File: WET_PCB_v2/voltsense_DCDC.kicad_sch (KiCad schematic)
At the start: 9 parts, among them J18 Capacitor connector, J20 Capacitor connector, U3 Opamp_Quad

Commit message: notees
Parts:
- removed D23, D24: 1N4004, Diode_THT:D_DO-15_P2.54mm_Vertical_CathodeUp, symbol Diode:1N4004
- added D29, D30: D_Zener, Diode_THT:D_DO-15_P2.54mm_Vertical_CathodeUp, symbol Device:D_Zener
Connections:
- net GND: now also D29.2 (A)
- net VDD_OPAMP: now also D30.1 (K)
- net Vsense_ADC: now also D29.1 (K), D30.2 (A)
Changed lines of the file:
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@@
+	)
+	(symbol
+		(lib_id "Device:D_Zener")
+		(at 121.92 58.42 270)
+		(unit 1)
+		(body_style 1)
+		(exclude_from_sim no)
+		(in_bom yes)
+		(on_board yes)
+		(in_pos_files yes)
+		(dnp no)
+		(fields_autoplaced yes)
+		(property "Reference" "D30"
+			(at 124.46 57.1499 90)
+			(show_name no)
+			(do_not_autoplace no)
+			(effects
+				(font
+					(size 1.27 1.27)
+				)
+				(justify left)
+			)
+		)
+		(property "Value" "D_Zener"
+			(at 124.46 59.6899 90)
+			(show_name no)
+			(do_not_autoplace no)
+			(effects
+				(font
+					(size 1.27 1.27)
+				)
+				(justify left)
+			)
+		)
+		(property "Footprint" "Diode_THT:D_DO-15_P2.54mm_Vertical_CathodeUp"
+			(at 121.92 58.42 0)
+			(hide yes)
+			(show_name no)
+			(do_not_autoplace no)
+			(effects
+				(font
+					(size 1.27 1.27)
+				)
+			)
+		)
+		(property "Datasheet" ""
+			(at 121.92 58.42 0)
+			(hide yes)
+			(show_name no)
+			(do_not_autoplace no)
+			(effects
+				(font
+					(size 1.27 1.27)
+				)
+			)
+		)
+		(property "Description" "Zener diode"
+			(at 121.92 58.42 0)
+			(hide yes)
+			(show_name no)
+			(do_not_autoplace no)
+			(effects
+				(font
+					(size 1.27 1.27)
+				)
+			)
+		)
+		(pin "2"
+		)
+		(pin "1"
+		)
+		(instances
+			(project "WET_PCB_v2"
+				(path "/13451c35-1666-47d9-9525-8d8125ba1cf3/a17383a4-d27f-4c25-9e0c-b0df1856b8d8"
+					(reference "D30")
+					(unit 1)
+				)
+			)
+		)
 	)
 	(symbol
@@
 				(path "/13451c35-1666-47d9-9525-8d8125ba1cf3/a17383a4-d27f-4c25-9e0c-b0df1856b8d8"
 					(reference "#PWR056")
-					(unit 1)
-				)
-			)
-		)
-	)
-	(symbol
-		(lib_id "Diode:1N4004")
-		(at 121.92 68.58 90)
-		(mirror x)
-		(unit 1)
-		(body_style 1)
-		(exclude_from_sim no)
-		(in_bom yes)
-		(on_board yes)
-		(in_pos_files yes)
-		(dnp no)
-		(fields_autoplaced yes)
-		(property "Reference" "D24"
-			(at 124.46 67.3099 90)
-			(show_name no)
-			(do_not_autoplace no)
-			(effects
-				(font
-					(size 1.27 1.27)
-				)
-				(justify right)
-			)
-		)
-		(property "Value" "1N4004"
-			(at 124.46 69.8499 90)
-			(show_name no)
-			(do_not_autoplace no)
-			(effects
-				(font
-					(size 1.27 1.27)
-				)
-				(justify right)
-			)
-		)
-		(property "Footprint" "Diode_THT:D_DO-15_P2.54mm_Vertical_CathodeUp"
-			(at 126.365 68.58 0)
-			(hide yes)
-			(show_name no)
-			(do_not_autoplace no)
-			(effects
-				(font
-					(size 1.27 1.27)
-				)
-			)
-		)
-		(property "Datasheet" "http://www.vishay.com/docs/88503/1n4001.pdf"
-			(at 121.92 68.58 0)
-			(hide yes)
-			(show_name no)
-			(do_not_autoplace no)
-			(effects
-				(font
-					(size 1.27 1.27)
-				)
-			)
-		)
-		(property "Description" "400V 1A General Purpose Rectifier Diode, DO-41"
-			(at 121.92 68.58 0)
-			(hide yes)
-			(show_name no)
-			(do_not_autoplace no)
-			(effects
-				(font
-					(size 1.27 1.27)
-				)
-			)
-		)
-		(property "Sim.Device" "D"
-			(at 121.92 68.58 0)
-			(hide yes)
-			(show_name no)
-			(do_not_autoplace no)
-			(effects
-				(font
-					(size 1.27 1.27)
-				)
-			)
-		)
-		(property "Sim.Pins" "1=K 2=A"
-			(at 121.92 68.58 0)
-			(hide yes)
-			(show_name no)
-			(do_not_autoplace no)
-			(effects
-				(font
-					(size 1.27 1.27)
-				)
-			)
-		)
-		(pin "1"
-		)
-		(pin "2"
-		)
-		(instances
-			(project "WET_PCB_v2"
-				(path "/13451c35-1666-47d9-9525-8d8125ba1cf3/a17383a4-d27f-4c25-9e0c-b0df1856b8d8"
-					(reference "D24")
 					(unit 1)
 				)
@@
 	)
 	(symbol
+		(lib_id "Device:D_Zener")
+		(at 121.92 68.58 270)
+		(unit 1)
+		(body_style 1)
+		(exclude_from_sim no)
+		(in_bom yes)
+		(on_board yes)
+		(in_pos_files yes)
+		(dnp no)
+		(fields_autoplaced yes)
+		(property "Reference" "D29"
+			(at 124.46 67.3099 90)
+			(show_name no)
+			(do_not_autoplace no)
+			(effects
+				(font
+					(size 1.27 1.27)
+				)
+				(justify left)
+			)
+		)
+		(property "Value" "D_Zener"
+			(at 124.46 69.8499 90)
+			(show_name no)
+			(do_not_autoplace no)
+			(effects
+				(font
+					(size 1.27 1.27)
+				)
+				(justify left)
+			)
+		)
+		(property "Footprint" "Diode_THT:D_DO-15_P2.54mm_Vertical_CathodeUp"
+			(at 121.92 68.58 0)
+			(hide yes)
+			(show_name no)
+			(do_not_autoplace no)
+			(effects
+				(font
+					(size 1.27 1.27)
+				)
+			)
+		)
+		(property "Datasheet" ""
+			(at 121.92 68.58 0)
+			(hide yes)
+			(show_name no)
+			(do_not_autoplace no)
+			(effects
+				(font
+					(size 1.27 1.27)
+				)
+			)
+		)
+		(property "Description" "Zener diode"
+			(at 121.92 68.58 0)
+			(hide yes)
+			(show_name no)
+			(do_not_autoplace no)
+			(effects
+				(font
+					(size 1.27 1.27)
+				)
+			)
+		)
+		(pin "2"
+		)
+		(pin "1"
+		)
+		(instances
+			(project "WET_PCB_v2"
+				(path "/13451c35-1666-47d9-9525-8d8125ba1cf3/a17383a4-d27f-4c25-9e0c-b0df1856b8d8"
+					(reference "D29")
+					(unit 1)
+				)
+			)
+		)
+	)
+	(symbol
 		(lib_id "power:GND")
 		(at 55.88 77.47 0)
@@
 					(unit 1)
 				)
-			)
-		)
-	)
-	(symbol
-		(lib_id "Diode:1N4004")
-		(at 121.92 58.42 90)
-		(mirror x)
-		(unit 1)
-		(body_style 1)
-		(exclude_from_sim no)
-		(in_bom yes)
-		(on_board yes)
-		(in_pos_files yes)
-		(dnp no)
-		(fields_autoplaced yes)
-		(property "Reference" "D23"
-			(at 124.46 57.1499 90)
-			(show_name no)
-			(do_not_autoplace no)
-			(effects
-				(font
-					(size 1.27 1.27)
-				)
-				(justify right)
-			)
-		)
-		(property "Value" "1N4004"
-			(at 124.46 59.6899 90)
-			(show_name no)
-			(do_not_autoplace no)
-			(effects
-				(font
-					(size 1.27 1.27)
-				)
-				(justify right)
-			)
-		)
-		(property "Footprint" "Diode_THT:D_DO-15_P2.54mm_Vertical_CathodeUp"
-			(at 126.365 58.42 0)
-			(hide yes)
-			(show_name no)
-			(do_not_autoplace no)
-			(effects
-				(font
-					(size 1.27 1.27)
-				)
-			)
-		)
-		(property "Datasheet" "http://www.vishay.com/docs/88503/1n4001.pdf"
-			(at 121.92 58.42 0)
-			(hide yes)
-			(show_name no)
-			(do_not_autoplace no)
-			(effects
-				(font
-					(size 1.27 1.27)
-				)
-			)
-		)
-		(property "Description" "400V 1A General Purpose Rectifier Diode, DO-41"
-			(at 121.92 58.42 0)
-			(hide yes)
-			(show_name no)
-			(do_not_autoplace no)
-			(effects
-				(font
-					(size 1.27 1.27)
-				)
-			)
-		)
-		(property "Sim.Device" "D"
-			(at 121.92 58.42 0)
-			(hide yes)
-			(show_name no)
-			(do_not_autoplace no)
-			(effects
-				(font
-					(size 1.27 1.27)
-				)
-			)
-		)
-		(property "Sim.Pins" "1=K 2=A"
-			(at 121.92 58.42 0)
-			(hide yes)
-			(show_name no)
-			(do_not_autoplace no)
-			(effects
-				(font
-					(size 1.27 1.27)
-				)
-			)
-		)
-		(pin "1"
-		)
-		(pin "2"
-		)
-		(instances
-			(project "WET_PCB_v2"
-				(path "/13451c35-1666-47d9-9525-8d8125ba1cf3/a17383a4-d27f-4c25-9e0c-b0df1856b8d8"
-					(reference "D23")
-					(unit 1)
-				)

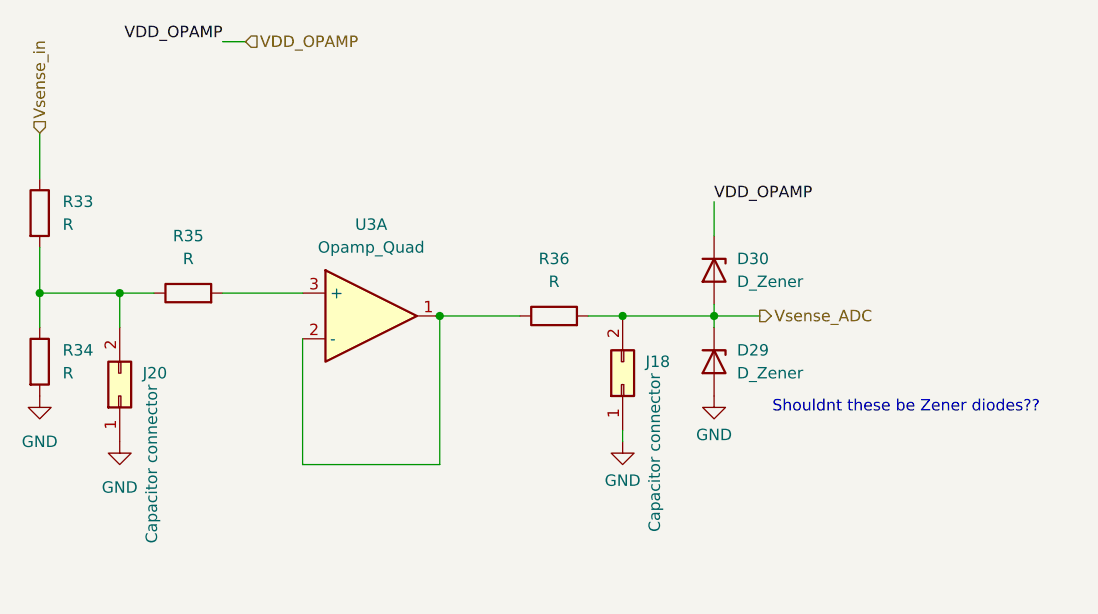
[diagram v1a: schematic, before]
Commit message: redid part of layout inverter
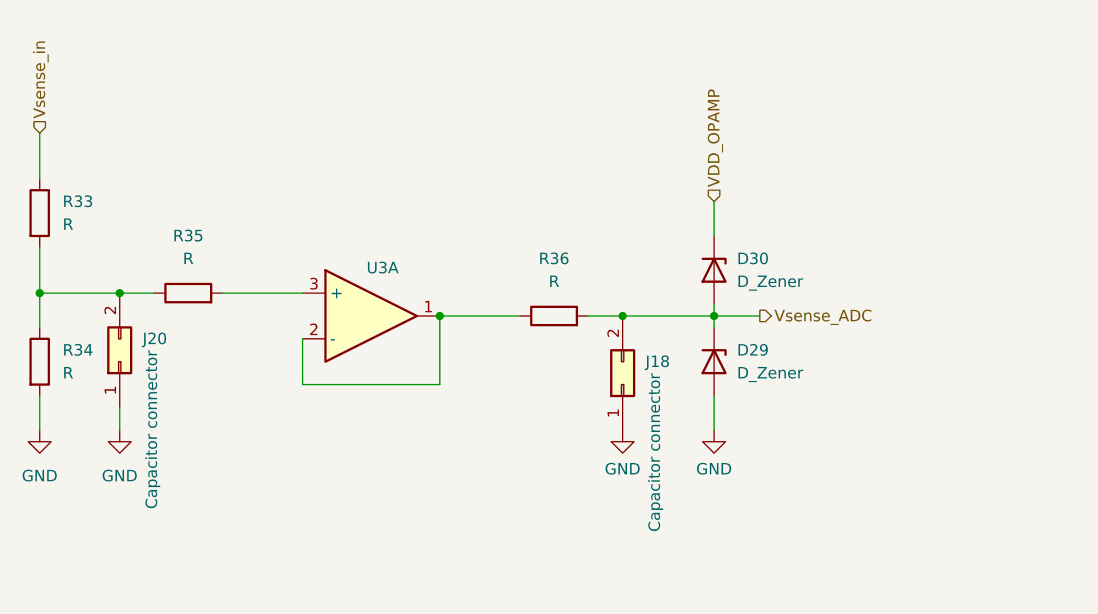
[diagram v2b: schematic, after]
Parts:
- R33, R34, R35, R36: footprint Resistor_THT:R_Axial_DIN0207_L6.3mm_D2.5mm_P7.62mm_Horizontal -> Resistor_SMD:R_0805_2012Metric_Pad1.20x1.40mm_HandSolder
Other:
- note removed: "Shouldnt these be Zener diodes??"
- moved on the sheet: J20
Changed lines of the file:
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@@
 	(generator_version "10.0")
 	(paper "A4")
-	(text "Shouldnt these be Zener diodes??\n"
-		(exclude_from_sim no)
-		(at 143.256 73.66 0)
-		(effects
-			(font
-				(size 1.27 1.27)
-			)
-		)
+	(junction
+		(at 121.92 63.5)
+		(diameter 0)
+		(color 0 0 0 0)
+	)
+	(junction
+		(at 91.44 63.5)
+		(diameter 0)
+		(color 0 0 0 0)
+	)
+	(junction
+		(at 111.76 63.5)
+		(diameter 0)
+		(color 0 0 0 0)
+	)
+	(junction
+		(at 46.99 60.96)
+		(diameter 0)
+		(color 0 0 0 0)
 	)
 	(junction
@@
 		(color 0 0 0 0)
 	)
-	(junction
-		(at 121.92 63.5)
-		(diameter 0)
-		(color 0 0 0 0)
-	)
-	(junction
-		(at 91.44 63.5)
-		(diameter 0)
-		(color 0 0 0 0)
-	)
-	(junction
-		(at 111.76 63.5)
-		(diameter 0)
-		(color 0 0 0 0)
-	)
-	(junction
-		(at 46.99 60.96)
-		(diameter 0)
-		(color 0 0 0 0)
-	)
-	(wire
-		(pts
-			(xy 91.44 63.5) (xy 91.44 80.01)
-		)
-		(stroke
-			(width 0)
-			(type default)
-		)
-	)
-	(wire
-		(pts
-			(xy 69.85 33.02) (xy 67.31 33.02)
+	(wire
+		(pts
+			(xy 46.99 72.39) (xy 46.99 76.2)
+		)
+		(stroke
+			(width 0)
+			(type default)
+		)
+	)
+	(wire
+		(pts
+			(xy 91.44 63.5) (xy 91.44 71.12)
 		)
 		(stroke
@@
 	(wire
 		(pts
+			(xy 55.88 73.66) (xy 55.88 76.2)
+		)
+		(stroke
+			(width 0)
+			(type default)
+		)
+	)
+	(wire
+		(pts
 			(xy 121.92 50.8) (xy 121.92 54.61)
 		)
@@
 	(wire
 		(pts
-			(xy 55.88 60.96) (xy 55.88 64.77)
-		)
-		(stroke
-			(width 0)
-			(type default)
-		)
-	)
-	(wire
-		(pts
 			(xy 121.92 63.5) (xy 121.92 64.77)
 		)
@@
 	(wire
 		(pts
-			(xy 111.76 76.2) (xy 111.76 77.47)
-		)
-		(stroke
-			(width 0)
-			(type default)
-		)
-	)
-	(wire
-		(pts
 			(xy 55.88 60.96) (xy 59.69 60.96)
 		)
@@
 	(wire
 		(pts
+			(xy 121.92 76.2) (xy 121.92 72.39)
+		)
+		(stroke
+			(width 0)
+			(type default)
+		)
+	)
+	(wire
+		(pts
 			(xy 111.76 63.5) (xy 121.92 63.5)
 		)
@@
 	(wire
 		(pts
-			(xy 76.2 66.04) (xy 76.2 80.01)
-		)
-		(stroke
-			(width 0)
-			(type default)
-		)
-	)
-	(wire
-		(pts
-			(xy 76.2 80.01) (xy 91.44 80.01)
-		)
-		(stroke
-			(width 0)
-			(type default)
-		)
-	)
-	(label "VDD_OPAMP"
-		(at 67.31 33.02 180)
-		(effects
-			(font
-				(size 1.27 1.27)
-			)
-			(justify right bottom)
-		)
-	)
-	(label "VDD_OPAMP"
-		(at 121.92 50.8 0)
-		(effects
-			(font
-				(size 1.27 1.27)
-			)
-			(justify left bottom)
+			(xy 76.2 66.04) (xy 76.2 71.12)
+		)
+		(stroke
+			(width 0)
+			(type default)
+		)
+	)
+	(wire
+		(pts
+			(xy 76.2 71.12) (xy 91.44 71.12)
+		)
+		(stroke
+			(width 0)
+			(type default)
 		)
 	)
@@
 	(hierarchical_label "VDD_OPAMP"
 		(shape input)
-		(at 69.85 33.02 0)
+		(at 121.92 50.8 90)
 		(effects
 			(font
@@
 	(symbol
 		(lib_id "power:GND")
-		(at 121.92 72.39 0)
+		(at 121.92 76.2 0)
 		(unit 1)
 		(body_style 1)
@@
 		(dnp no)
 		(property "Reference" "#PWR056"
-			(at 121.92 78.74 0)
+			(at 121.92 82.55 0)
 			(hide yes)
 			(show_name no)
@@
 		)
 		(property "Value" "GND"
-			(at 121.92 76.708 0)
+			(at 121.92 80.518 0)
 			(show_name no)
 			(do_not_autoplace no)
@@
 		)
 		(property "Footprint" ""
-			(at 121.92 72.39 0)
+			(at 121.92 76.2 0)
 			(hide yes)
 			(show_name no)
@@
 		)
 		(property "Datasheet" ""
-			(at 121.92 72.39 0)
+			(at 121.92 76.2 0)
 			(hide yes)
 			(show_name no)
@@
 		)
 		(property "Description" "Power symbol creates a global label with name \"GND\" , ground"
-			(at 121.92 72.39 0)
+			(at 121.92 76.2 0)
 			(hide yes)
 			(show_name no)
@@
 			)
 		)
-		(property "Footprint" "Resistor_THT:R_Axial_DIN0207_L6.3mm_D2.5mm_P7.62mm_Horizontal"
+		(property "Footprint" "Resistor_SMD:R_0805_2012Metric_Pad1.20x1.40mm_HandSolder"
 			(at 45.212 68.58 90)
 			(hide yes)
@@
 	(symbol
 		(lib_id "power:GND")
-		(at 55.88 77.47 0)
+		(at 55.88 76.2 0)
 		(unit 1)
 		(body_style 1)
@@
 		(fields_autoplaced yes)
 		(property "Reference" "#PWR054"
-			(at 55.88 83.82 0)
+			(at 55.88 82.55 0)
 			(hide yes)
 			(show_name no)
@@
 		)
 		(property "Value" "GND"
-			(at 55.88 82.55 0)
+			(at 55.88 81.28 0)
 			(show_name no)
 			(do_not_autoplace no)
@@
 		)
 		(property "Footprint" ""
-			(at 55.88 77.47 0)
+			(at 55.88 76.2 0)
 			(hide yes)
 			(show_name no)
@@
 		)
 		(property "Datasheet" ""
-			(at 55.88 77.47 0)
+			(at 55.88 76.2 0)
 			(hide yes)
 			(show_name no)
@@
 		)
 		(property "Description" "Power symbol creates a global label with name \"GND\" , ground"
-			(at 55.88 77.47 0)
+			(at 55.88 76.2 0)
 			(hide yes)
 			(show_name no)
@@
 			)
 		)
-		(property "Footprint" "Resistor_THT:R_Axial_DIN0207_L6.3mm_D2.5mm_P7.62mm_Horizontal"
+		(property "Footprint" "Resistor_SMD:R_0805_2012Metric_Pad1.20x1.40mm_HandSolder"
 			(at 63.5 62.738 90)
 			(hide yes)
@@
 	(symbol
 		(lib_id "Connector_Generic:Conn_02x01")
-		(at 55.88 72.39 90)
+		(at 55.88 68.58 90)
 		(unit 1)
 		(body_style 1)
@@
 		(dnp no)
 		(property "Reference" "J20"
-			(at 58.42 69.8499 90)
+			(at 58.42 66.0399 90)
 			(show_name no)
 			(do_not_autoplace no)
@@
 		)
 		(property "Value" "Capacitor connector"
-			(at 59.436 71.12 0)
+			(at 59.436 67.31 0)
 			(show_name no)
 			(do_not_autoplace no)
@@
 		)
 		(property "Footprint" "Connector_PinSocket_2.54mm:PinSocket_1x02_P2.54mm_Vertical"
-			(at 55.88 72.39 0)
+			(at 55.88 68.58 0)
 			(hide yes)
 			(show_name no)
@@
 		)
 		(property "Datasheet" ""
-			(at 55.88 72.39 0)
+			(at 55.88 68.58 0)
 			(hide yes)
 			(show_name no)
@@
 		)
 		(property "Description" "Generic connector, double row, 02x01, this symbol is compatible with counter-clockwise, top-bottom and odd-even numbering schemes., script generated (kicad-library-utils/schlib/autogen/connector/)"
-			(at 55.88 72.39 0)
+			(at 55.88 68.58 0)
 			(hide yes)
 			(show_name no)
@@
 			)
 		)
-		(property "Footprint" "Resistor_THT:R_Axial_DIN0207_L6.3mm_D2.5mm_P7.62mm_Horizontal"
+		(property "Footprint" "Resistor_SMD:R_0805_2012Metric_Pad1.20x1.40mm_HandSolder"
 			(at 104.14 65.278 90)
 			(hide yes)
@@
 		(in_pos_files yes)
 		(dnp no)
-		(fields_autoplaced yes)
 		(property "Reference" "U3"
-			(at 83.82 53.34 0)
+			(at 85.09 58.166 0)
 			(show_name no)
 			(do_not_autoplace no)
@@
 		(property "Value" "Opamp_Quad"
 			(at 83.82 55.88 0)
+			(hide yes)
 			(show_name no)
 			(do_not_autoplace no)
@@
 			)
 		)
-		(property "Footprint" "Resistor_THT:R_Axial_DIN0207_L6.3mm_D2.5mm_P7.62mm_Horizontal"
+		(property "Footprint" "Resistor_SMD:R_0805_2012Metric_Pad1.20x1.40mm_HandSolder"
 			(at 45.212 52.07 90)
 			(hide yes)
@@
 	(symbol
 		(lib_id "power:GND")
-		(at 111.76 77.47 0)
+		(at 111.76 76.2 0)
 		(unit 1)
 		(body_style 1)
@@
 		(dnp no)
 		(property "Reference" "#PWR055"
-			(at 111.76 83.82 0)
+			(at 111.76 82.55 0)
 			(hide yes)
 			(show_name no)
@@
 		)
 		(property "Value" "GND"
-			(at 111.76 81.788 0)
+			(at 111.76 80.518 0)
 			(show_name no)
 			(do_not_autoplace no)
@@
 		)
 		(property "Footprint" ""
-			(at 111.76 77.47 0)
+			(at 111.76 76.2 0)
 			(hide yes)
 			(show_name no)
@@
 		)
 		(property "Datasheet" ""
-			(at 111.76 77.47 0)
+			(at 111.76 76.2 0)
 			(hide yes)
 			(show_name no)
@@
 		)
 		(property "Description" "Power symbol creates a global label with name \"GND\" , ground"
-			(at 111.76 77.47 0)
+			(at 111.76 76.2 0)
 			(hide yes)
 			(show_name no)
@@
 	(symbol
 		(lib_id "power:GND")
-		(at 46.99 72.39 0)
+		(at 46.99 76.2 0)
 		(unit 1)
 		(body_style 1)
@@
 		(fields_autoplaced yes)
 		(property "Reference" "#PWR020"
-			(at 46.99 78.74 0)
+			(at 46.99 82.55 0)
 			(hide yes)
 			(show_name no)
@@
 		)
 		(property "Value" "GND"
-			(at 46.99 77.47 0)
+			(at 46.99 81.28 0)
 			(show_name no)
 			(do_not_autoplace no)
@@
 		)
 		(property "Footprint" ""
-			(at 46.99 72.39 0)
+			(at 46.99 76.2 0)
 			(hide yes)
 			(show_name no)
@@
 		)
 		(property "Datasheet" ""
-			(at 46.99 72.39 0)
+			(at 46.99 76.2 0)
 			(hide yes)
 			(show_name no)
@@
 		)
 		(property "Description" "Power symbol creates a global label with name \"GND\" , ground"
-			(at 46.99 72.39 0)
-			(hide yes)
-			(show_name no)
+			(at 46.99 76.2 0)
+			(hide yes)
+			(show_name no)

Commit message: didnt watch the lecture but made progress ig
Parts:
- added R42: R0, Resistor_SMD:R_0805_2012Metric_Pad1.20x1.40mm_HandSolder, symbol Device:R
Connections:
- net at R36.1, U3.1: now also R42.2; no longer U3.2 (-)
- new net: R42.1, U3.2 (-)
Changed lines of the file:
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@@
+	(wire
+		(pts
+			(xy 76.2 71.12) (xy 80.01 71.12)
+		)
+		(stroke
+			(width 0)
+			(type default)
+		)
+	)
 	(wire
 		(pts
@@
 	(wire
 		(pts
-			(xy 46.99 55.88) (xy 46.99 60.96)
+			(xy 87.63 71.12) (xy 91.44 71.12)
 		)
 		(stroke
@@
 	(wire
 		(pts
-			(xy 91.44 63.5) (xy 100.33 63.5)
+			(xy 46.99 55.88) (xy 46.99 60.96)
 		)
 		(stroke
@@
 	(wire
 		(pts
-			(xy 121.92 63.5) (xy 127 63.5)
+			(xy 91.44 63.5) (xy 100.33 63.5)
 		)
 		(stroke
@@
 	(wire
 		(pts
-			(xy 121.92 76.2) (xy 121.92 72.39)
+			(xy 121.92 63.5) (xy 127 63.5)
 		)
 		(stroke
@@
 	(wire
 		(pts
-			(xy 111.76 63.5) (xy 121.92 63.5)
+			(xy 121.92 76.2) (xy 121.92 72.39)
 		)
 		(stroke
@@
 	(wire
 		(pts
-			(xy 76.2 66.04) (xy 76.2 71.12)
+			(xy 111.76 63.5) (xy 121.92 63.5)
 		)
 		(stroke
@@
 	(wire
 		(pts
-			(xy 76.2 71.12) (xy 91.44 71.12)
+			(xy 76.2 66.04) (xy 76.2 71.12)
 		)
 		(stroke
@@
 					(unit 1)
 				)
+			)
+		)
+	)
+	(symbol
+		(lib_id "Device:R")
+		(at 83.82 71.12 90)
+		(unit 1)
+		(body_style 1)
+		(exclude_from_sim no)
+		(in_bom yes)
+		(on_board yes)
+		(in_pos_files yes)
+		(dnp no)
+		(fields_autoplaced yes)
+		(property "Reference" "R42"
+			(at 83.82 64.77 90)
+			(show_name no)
+			(do_not_autoplace no)
+			(effects
+				(font
+					(size 1.27 1.27)
+				)
+			)
+		)
+		(property "Value" "R0"
+			(at 83.82 67.31 90)
+			(show_name no)
+			(do_not_autoplace no)
+			(effects
+				(font
+					(size 1.27 1.27)
+				)
+			)
+		)
+		(property "Footprint" "Resistor_SMD:R_0805_2012Metric_Pad1.20x1.40mm_HandSolder"
+			(at 83.82 72.898 90)
+			(hide yes)
+			(show_name no)
+			(do_not_autoplace no)
+			(effects
+				(font
+					(size 1.27 1.27)
+				)
+			)
+		)
+		(property "Datasheet" ""
+			(at 83.82 71.12 0)
+			(hide yes)
+			(show_name no)
+			(do_not_autoplace no)
+			(effects
+				(font
+					(size 1.27 1.27)
+				)
+			)
+		)
+		(property "Description" "Resistor"
+			(at 83.82 71.12 0)
+			(hide yes)
+			(show_name no)
+			(do_not_autoplace no)
+			(effects
+				(font
+					(size 1.27 1.27)
+				)
+			)
+		)
+		(pin "2"
+		)
+		(pin "1"
+		)
+		(instances
+			(project "WET_PCB_v2"
+				(path "/13451c35-1666-47d9-9525-8d8125ba1cf3/a17383a4-d27f-4c25-9e0c-b0df1856b8d8"
+					(reference "R42")
+					(unit 1)
+				)
